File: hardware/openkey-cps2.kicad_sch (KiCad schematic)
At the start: 13 parts, among them CN9 Conn_01x06, J1 Solder Pad, U1 ATtinyxx4

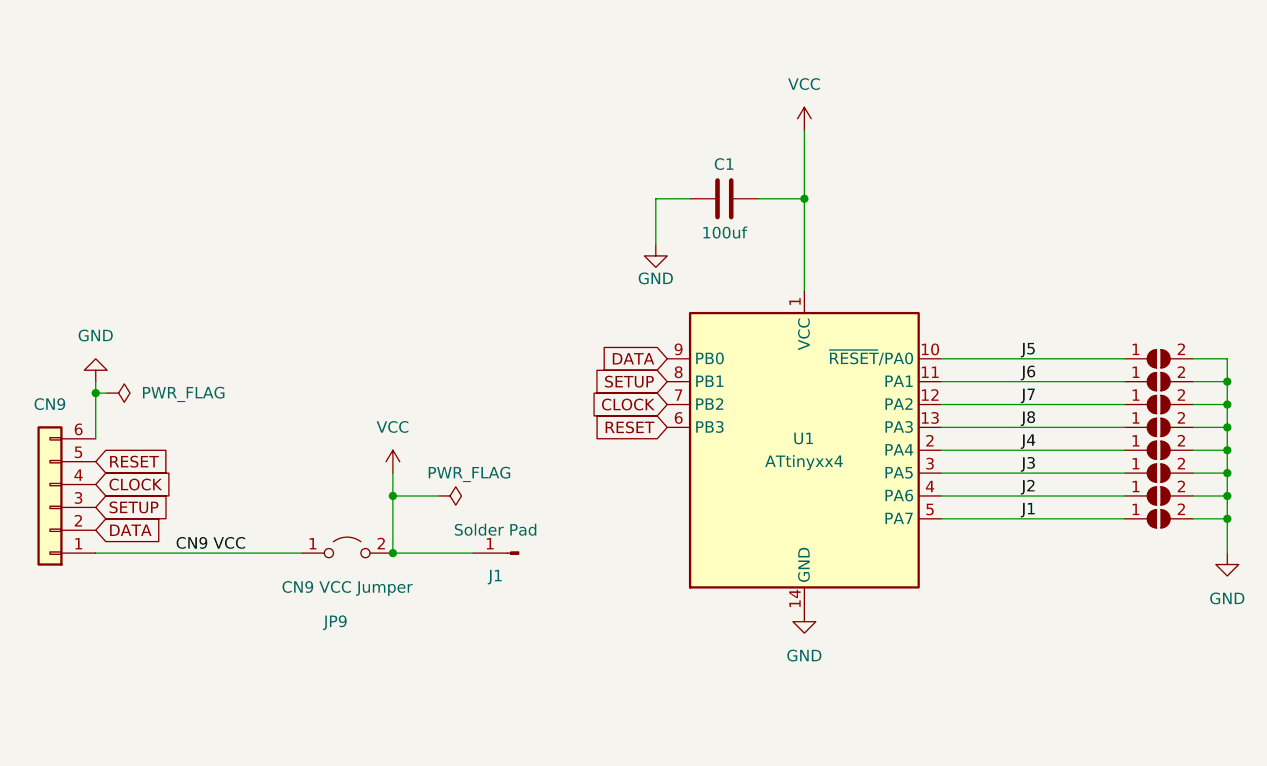
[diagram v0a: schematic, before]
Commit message: Initial support for 93646B-3/4 revision boards
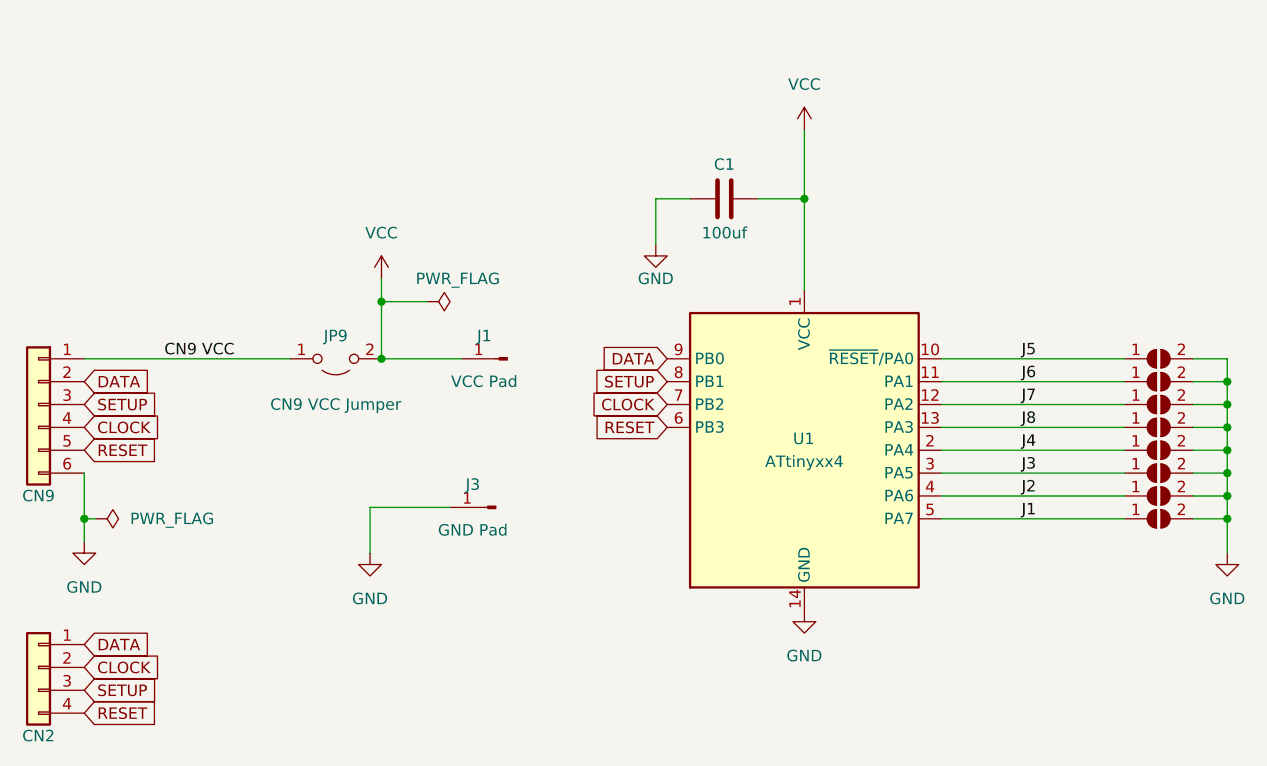
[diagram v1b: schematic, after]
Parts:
- added J2: CN2, Connector_PinHeader_2.54mm:PinHeader_1x04_P2.54mm_Vertical, symbol Connector_Generic:Conn_01x04
- added J3: GND Pad, TestPoint:TestPoint_Pad_D2.5mm, symbol Connector:Conn_01x01_Male
- J1: value Solder Pad -> VCC Pad
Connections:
- net CLOCK: now also J2.2 (Pin_2)
- net DATA: now also J2.1 (Pin_1)
- net GND: now also J3.1 (Pin_1)
- net RESET: now also J2.4 (Pin_4)
- net SETUP: now also J2.3 (Pin_3)
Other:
- moved on the sheet: CN9, J1, JP9

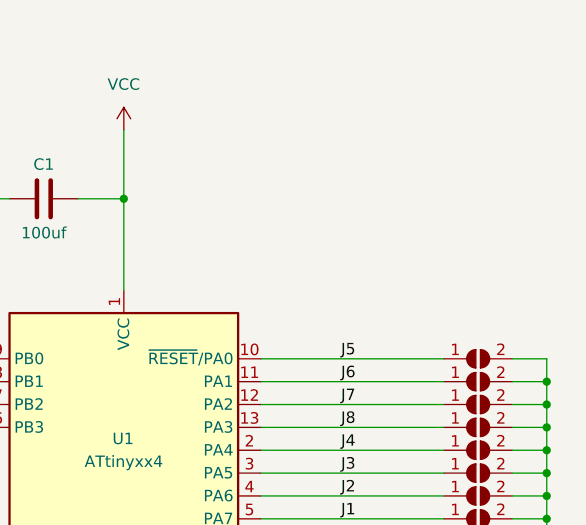
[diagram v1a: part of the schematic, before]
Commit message: HW: Add support for 93646B-3/4 and 97691A-3/4.  Add UPDI header.
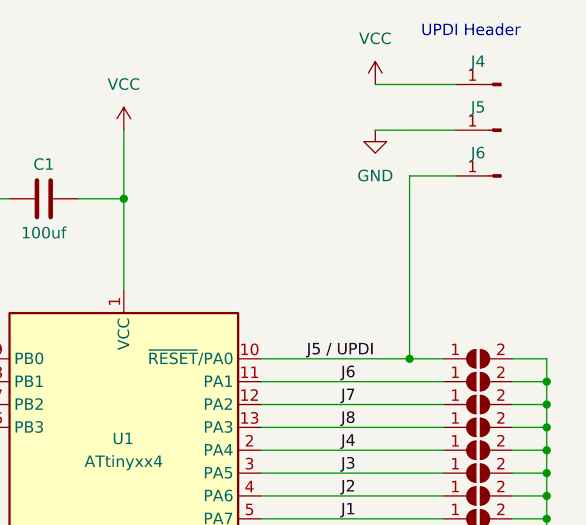
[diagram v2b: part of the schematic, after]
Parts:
- added J4: VCC, TestPoint:TestPoint_Pad_D1.5mm, symbol Connector:Conn_01x01_Male
- added J5: GND, TestPoint:TestPoint_Pad_D1.5mm, symbol Connector:Conn_01x01_Male
- added J6: J5 / UDPI, TestPoint:TestPoint_Pad_D1.5mm, symbol Connector:Conn_01x01_Male
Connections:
- net GND: now also J5.1 (Pin_1)
- net VCC: now also J4.1 (Pin_1)
- net J5 renamed J5 / UPDI
- net J5 / UPDI: now also J6.1 (Pin_1)
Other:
- note added: "UPDI Header"
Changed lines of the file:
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@@
   (junction (at 203.2 99.06) (diameter 0) (color 0 0 0 0)
   )
+  (junction (at 187.96 91.44) (diameter 0) (color 0 0 0 0)
+  )
   (junction (at 76.2 109.22) (diameter 0) (color 0 0 0 0)
   )
@@
     (stroke (width 0) (type default) (color 0 0 0 0))
   )
+  (wire (pts (xy 187.96 71.12) (xy 187.96 91.44))
+    (stroke (width 0) (type default) (color 0 0 0 0))
+  )
   (wire (pts (xy 203.2 106.68) (xy 203.2 109.22))
     (stroke (width 0) (type default) (color 0 0 0 0))
@@
     (stroke (width 0) (type default) (color 0 0 0 0))
   )
+  (wire (pts (xy 184.15 60.96) (xy 193.04 60.96))
+    (stroke (width 0) (type default) (color 0 0 0 0))
+  )
   (wire (pts (xy 171.45 93.98) (xy 191.77 93.98))
     (stroke (width 0) (type default) (color 0 0 0 0))
@@
     (stroke (width 0) (type default) (color 0 0 0 0))
   )
+  (wire (pts (xy 187.96 91.44) (xy 191.77 91.44))
+    (stroke (width 0) (type default) (color 0 0 0 0))
+  )
   (wire (pts (xy 171.45 96.52) (xy 191.77 96.52))
     (stroke (width 0) (type default) (color 0 0 0 0))
@@
     (stroke (width 0) (type default) (color 0 0 0 0))
   )
+  (wire (pts (xy 193.04 71.12) (xy 187.96 71.12))
+    (stroke (width 0) (type default) (color 0 0 0 0))
+  )
   (wire (pts (xy 139.7 73.66) (xy 139.7 78.74))
     (stroke (width 0) (type default) (color 0 0 0 0))
@@
     (stroke (width 0) (type default) (color 0 0 0 0))
   )
-  (wire (pts (xy 171.45 91.44) (xy 191.77 91.44))
+  (wire (pts (xy 171.45 91.44) (xy 187.96 91.44))
     (stroke (width 0) (type default) (color 0 0 0 0))
   )
@@
     (stroke (width 0) (type default) (color 0 0 0 0))
   )
+  (wire (pts (xy 184.15 66.04) (xy 193.04 66.04))
+    (stroke (width 0) (type default) (color 0 0 0 0))
+  )
   (wire (pts (xy 203.2 109.22) (xy 203.2 113.03))
     (stroke (width 0) (type default) (color 0 0 0 0))
@@
     (stroke (width 0) (type default) (color 0 0 0 0))
   )
+  (text "UPDI Header" (at 189.23 55.88 0)
+    (effects (font (size 1.27 1.27)) (justify left bottom))
+  )
   (label "J3" (at 180.34 104.14 0)
     (effects (font (size 1.27 1.27)) (justify left bottom))
@@
     (effects (font (size 1.27 1.27)) (justify left bottom))
   )
-  (label "J5" (at 180.34 91.44 0)
+  (label "J5 {slash} UPDI" (at 176.53 91.44 0)
     (effects (font (size 1.27 1.27)) (justify left bottom))
   )
@@
     )
     (property "Datasheet" "" (id 3) (at 76.2 111.76 0)
+      (effects (font (size 1.27 1.27)) hide)
+    )
+    (pin "1")
+  )
+  (symbol (lib_id "Connector:Conn_01x01_Male") (at 198.12 66.04 0) (mirror y) (unit 1)
+    (in_bom yes) (on_board yes)
+    (property "Reference" "J5" (id 0) (at 195.58 63.5 0))
+    (property "Value" "GND" (id 1) (at 195.58 68.58 0)
+      (effects (font (size 1.27 1.27)) hide)
+    )
+    (property "Footprint" "TestPoint:TestPoint_Pad_D1.5mm" (id 2) (at 198.12 66.04 0)
+      (effects (font (size 1.27 1.27)) hide)
+    )
+    (property "Datasheet" "~" (id 3) (at 198.12 66.04 0)
       (effects (font (size 1.27 1.27)) hide)
     )
@@
     (pin "1")
   )
+  (symbol (lib_id "Connector:Conn_01x01_Male") (at 198.12 60.96 0) (mirror y) (unit 1)
+    (in_bom yes) (on_board yes)
+    (property "Reference" "J4" (id 0) (at 195.58 58.42 0))
+    (property "Value" "VCC" (id 1) (at 195.58 63.5 0)
+      (effects (font (size 1.27 1.27)) hide)
+    )
+    (property "Footprint" "TestPoint:TestPoint_Pad_D1.5mm" (id 2) (at 198.12 60.96 0)
+      (effects (font (size 1.27 1.27)) hide)
+    )
+    (property "Datasheet" "~" (id 3) (at 198.12 60.96 0)
+      (effects (font (size 1.27 1.27)) hide)
+    )
+    (pin "1")
+  )
   (symbol (lib_id "Device:C") (at 147.32 73.66 90) (unit 1)
     (in_bom yes) (on_board yes)
@@
     (pin "2")
   )
+  (symbol (lib_id "power:VCC") (at 184.15 60.96 0) (unit 1)
+    (in_bom yes) (on_board yes) (fields_autoplaced)
+    (property "Reference" "#PWR03" (id 0) (at 184.15 64.77 0)
+      (effects (font (size 1.27 1.27)) hide)
+    )
+    (property "Value" "VCC" (id 1) (at 184.15 55.88 0))
+    (property "Footprint" "" (id 2) (at 184.15 60.96 0)
+      (effects (font (size 1.27 1.27)) hide)
+    )
+    (property "Datasheet" "" (id 3) (at 184.15 60.96 0)
+      (effects (font (size 1.27 1.27)) hide)
+    )
+    (pin "1")
+  )
   (symbol (lib_id "Connector:Conn_01x01_Male") (at 121.92 107.95 0) (mirror y) (unit 1)
     (in_bom yes) (on_board yes)
@@
     (pin "1")
   )
+  (symbol (lib_id "power:GND") (at 184.15 66.04 0) (unit 1)
+    (in_bom yes) (on_board yes) (fields_autoplaced)
+    (property "Reference" "#PWR04" (id 0) (at 184.15 72.39 0)
+      (effects (font (size 1.27 1.27)) hide)
+    )
+    (property "Value" "GND" (id 1) (at 184.15 71.12 0))
+    (property "Footprint" "" (id 2) (at 184.15 66.04 0)
+      (effects (font (size 1.27 1.27)) hide)
+    )
+    (property "Datasheet" "" (id 3) (at 184.15 66.04 0)
+      (effects (font (size 1.27 1.27)) hide)
+    )
+    (pin "1")
+  )
+  (symbol (lib_id "Connector:Conn_01x01_Male") (at 198.12 71.12 0) (mirror y) (unit 1)
+    (in_bom yes) (on_board yes)
+    (property "Reference" "J6" (id 0) (at 195.58 68.58 0))
+    (property "Value" "J5 / UDPI" (id 1) (at 195.58 73.66 0)
+      (effects (font (size 1.27 1.27)) hide)
+    )
+    (property "Footprint" "TestPoint:TestPoint_Pad_D1.5mm" (id 2) (at 198.12 71.12 0)
+      (effects (font (size 1.27 1.27)) hide)
+    )
+    (property "Datasheet" "~" (id 3) (at 198.12 71.12 0)
+      (effects (font (size 1.27 1.27)) hide)
+    )
+    (pin "1")
+  )
   (symbol (lib_id "Jumper:SolderJumper_2_Open") (at 195.58 109.22 0) (unit 1)
     (in_bom yes) (on_board yes) (fields_autoplaced)
@@
       (reference "#PWR02") (unit 1) (value "GND") (footprint "")
     )
+    (path "/d7302fa5-93a8-4f2b-a1b7-03bcc7f5b4bd"
+      (reference "#PWR03") (unit 1) (value "VCC") (footprint "")
+    )
+    (path "/dd29875b-8f86-47e8-bd74-f53e8b7a110e"
+      (reference "#PWR04") (unit 1) (value "GND") (footprint "")
+    )
     (path "/266f4ae6-6457-4c40-b280-b5853db2fd53"
       (reference "#PWR0101") (unit 1) (value "VCC") (footprint "")
@@
       (reference "J3") (unit 1) (value "GND Pad") (footprint "TestPoint:TestPoint_Pad_D2.5mm")
     )
+    (path "/cf0fbb7d-65a3-4bcc-b071-3b737f44ea19"
+      (reference "J4") (unit 1) (value "VCC") (footprint "TestPoint:TestPoint_Pad_D1.5mm")
+    )
+    (path "/4e04d2df-863f-404f-8327-4d9a6760e751"
+      (reference "J5") (unit 1) (value "GND") (footprint "TestPoint:TestPoint_Pad_D1.5mm")
+    )
+    (path "/e6429246-0ec1-4ce7-8bdc-caa21332c99e"
+      (reference "J6") (unit 1) (value "J5 / UDPI") (footprint "TestPoint:TestPoint_Pad_D1.5mm")
+    )
     (path "/b0196af3-d691-4c71-a0e4-9aed2403cf05"

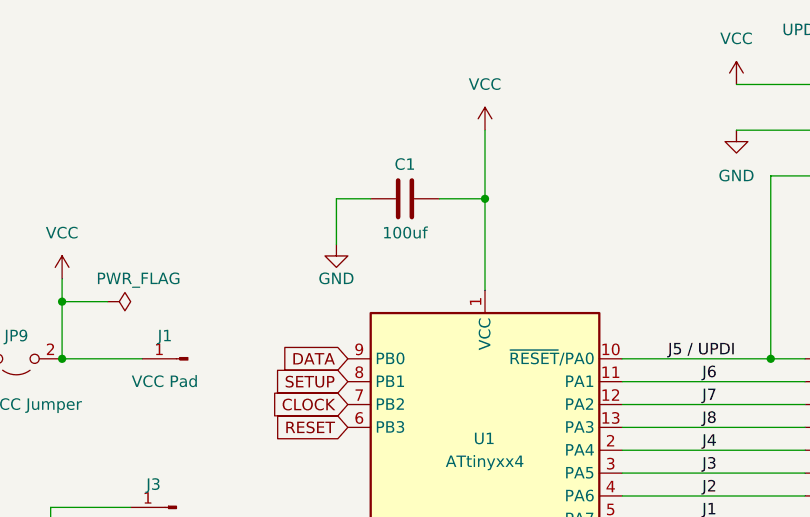
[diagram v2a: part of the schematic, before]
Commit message: HW: bypass cap value typo'd as 100uf when it should be 100nf
Thanks for hatmoose for pointing out the typo
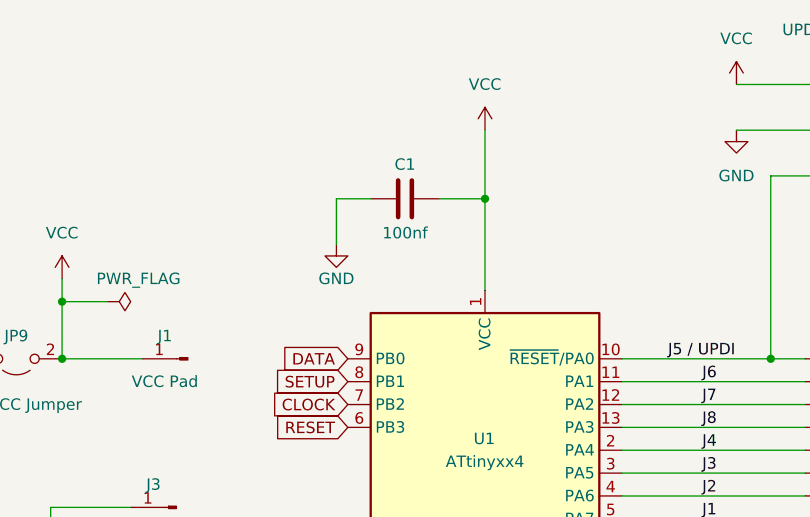
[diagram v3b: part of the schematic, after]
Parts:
- C1: value 100uf -> 100nf
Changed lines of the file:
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@@
     (in_bom yes) (on_board yes)
     (property "Reference" "C1" (id 0) (at 147.32 69.85 90))
-    (property "Value" "100uf" (id 1) (at 147.32 77.47 90))
+    (property "Value" "100nf" (id 1) (at 147.32 77.47 90))
     (property "Footprint" "openkey:C_0805_2012Metric_Pad1.18x1.45mm_HandSolder" (id 2) (at 151.13 72.6948 0)
       (effects (font (size 1.27 1.27)) hide)
@@
     )
     (path "/d070f14a-2712-4457-b433-72745d2bc776"
-      (reference "C1") (unit 1) (value "100uf") (footprint "openkey:C_0805_2012Metric_Pad1.18x1.45mm_HandSolder")
+      (reference "C1") (unit 1) (value "100nf") (footprint "openkey:C_0805_2012Metric_Pad1.18x1.45mm_HandSolder")
     )
     (path "/a88dd831-c7ee-430b-a2ad-2753391a8f94"

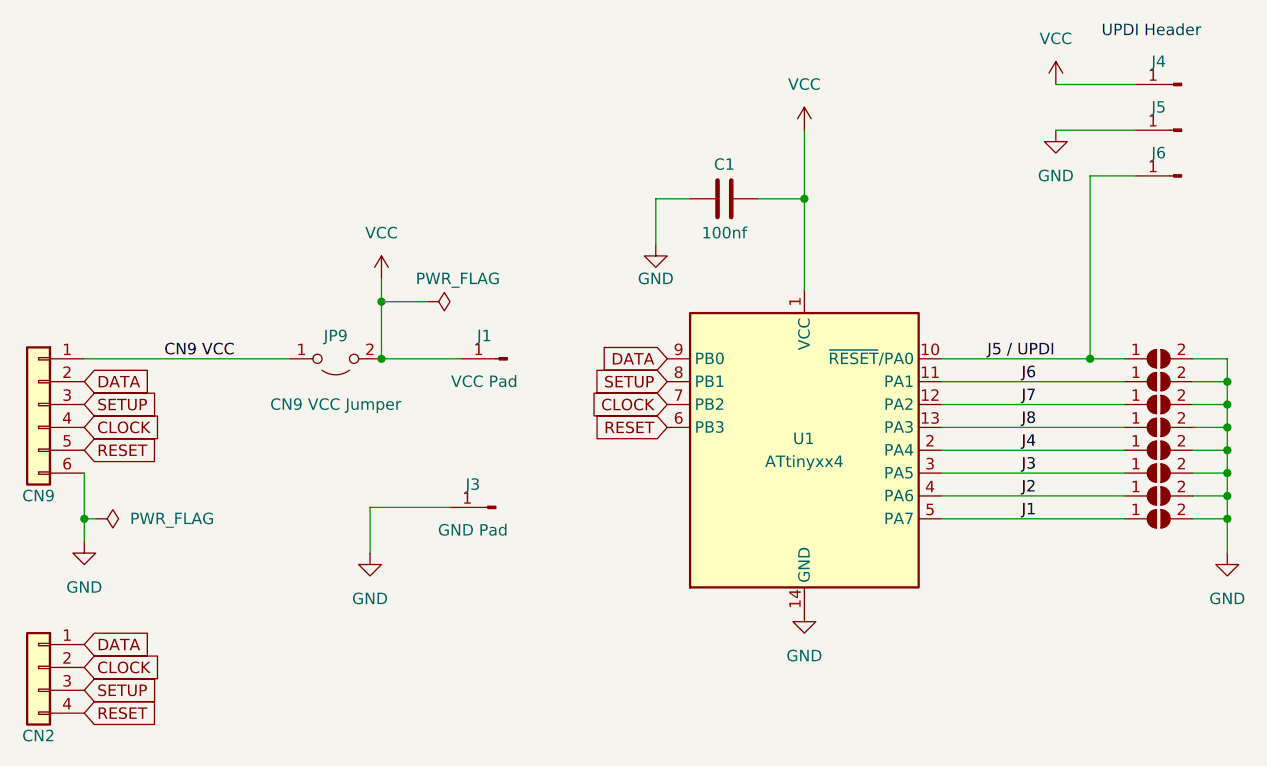
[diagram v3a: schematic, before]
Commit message: panel + assembly updates
- have kikit create the panel (was done by hand before)
- have jlcpcb fabrication plugin create bom/positions files for the panel
- create PANEL.md with instructions for having jlcpcb assemble the board
- update kicad files to 10.x
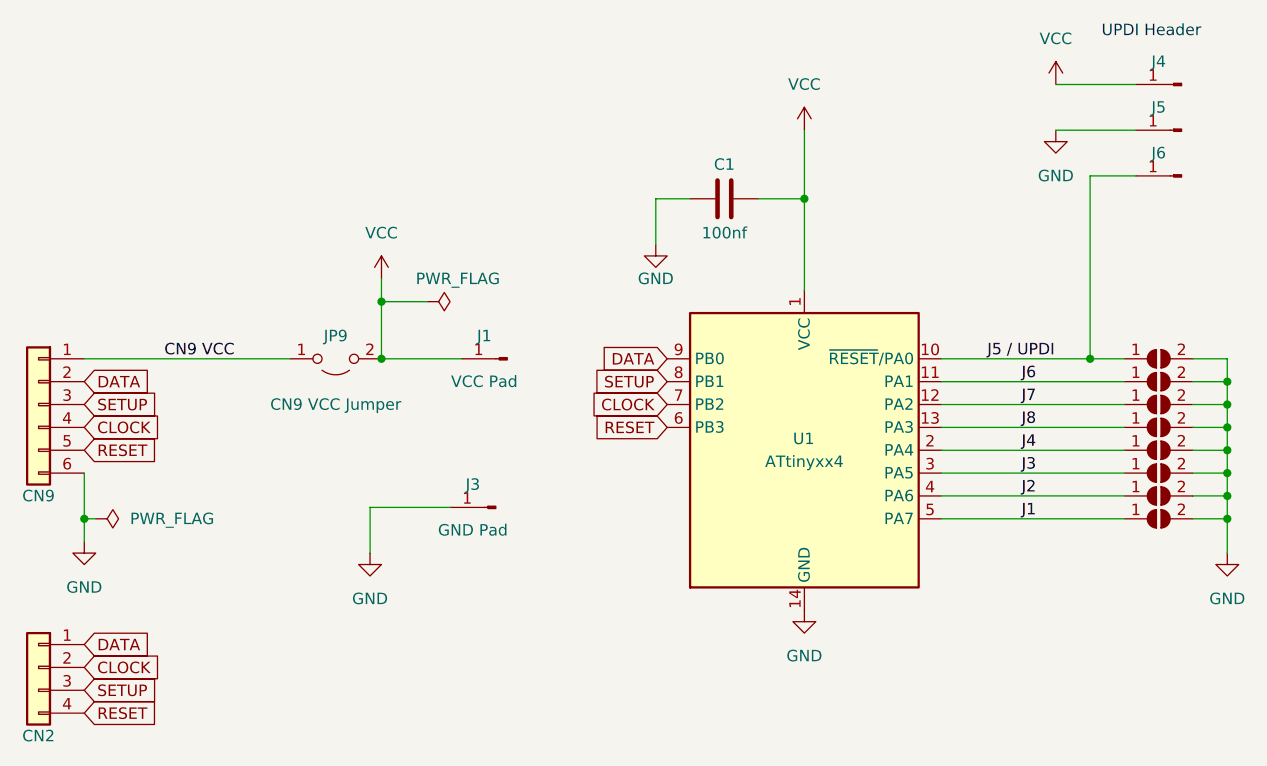
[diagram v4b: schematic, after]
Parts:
- C1: LCSC (none) -> C49678
- CN9, J1, J2, J3, J4, J5, J6, JP1, JP2, JP3, JP4, JP5, JP6, JP7, JP8, JP9: now left out of the parts list
- U1: LCSC (none) -> C1339119
